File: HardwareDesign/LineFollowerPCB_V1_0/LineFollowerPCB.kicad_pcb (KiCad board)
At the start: 2 copper layers, 152 x 100 mm, 16 parts, among them J1 B2B-XH-A, J2 B4B-XH-A, J3 Conn_01x04, J4 Conn_01x02_Socket, M1 Motor_DC, M2 Motor_DC, U1 Black Pill v2, U2 DRV8833, U3 AMS1117-3.3, U4 SX1308

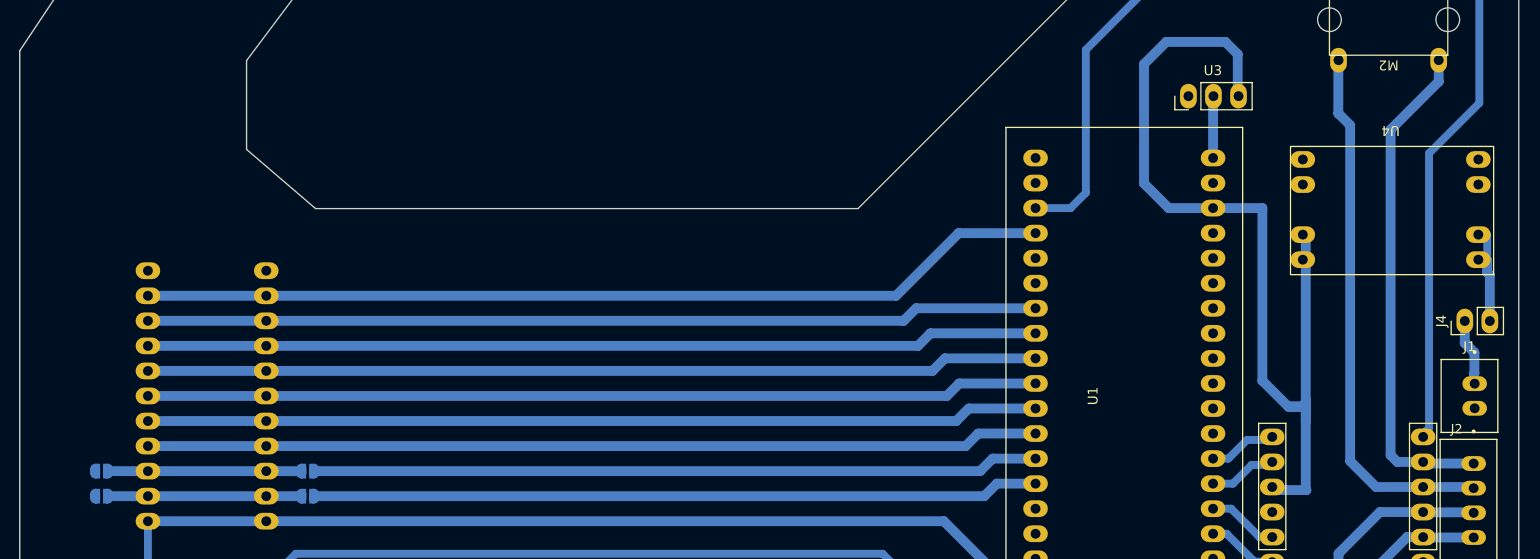
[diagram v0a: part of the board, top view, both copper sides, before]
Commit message: Add 1N4001 doide and connect the 5V power signal to the sensor
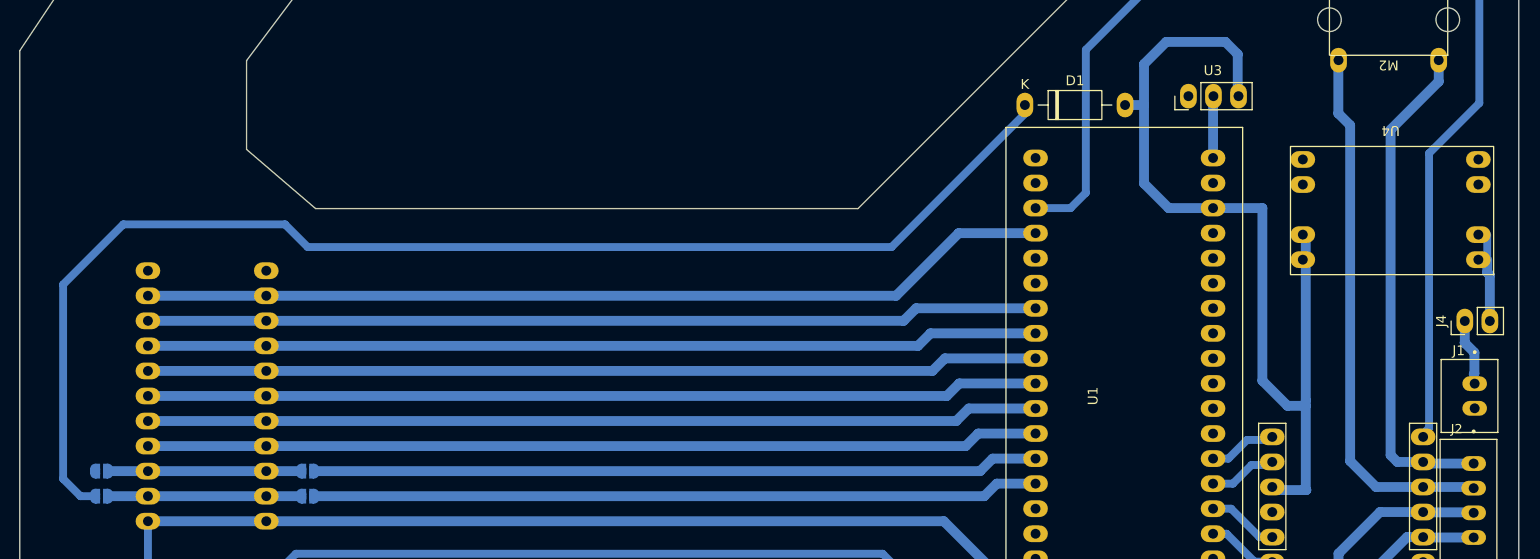
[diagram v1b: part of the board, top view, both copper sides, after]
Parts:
- added D1: 1N4001, Diode_THT:D_DO-41_SOD81_P10.16mm_Horizontal, F.Cu at (171.9, 59.5)
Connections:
- JP2 pad 1: 5.5V -> Net-(D1-K)
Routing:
- net Net-(D1-K): track 0.00 -> 131.2 mm
- net 5.5V: track 96.7 -> 94.9 mm

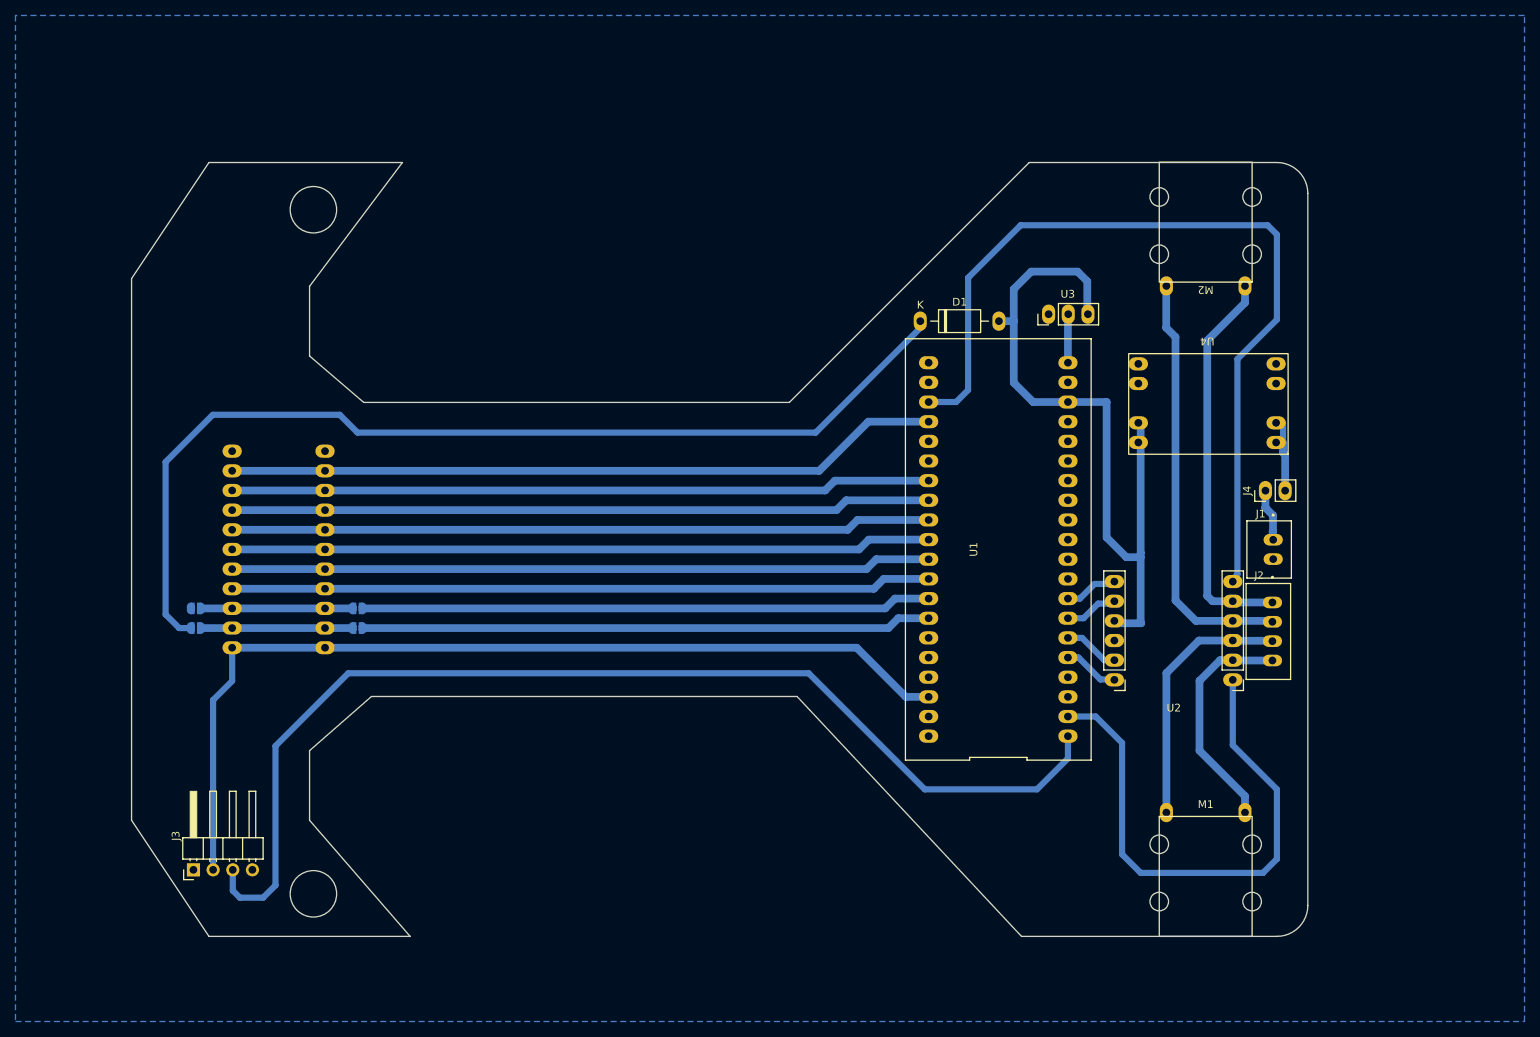
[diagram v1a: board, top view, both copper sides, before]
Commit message: Hardware changes: - Change the Neopixel pin to B15 instead of B12 - Add IR pinheader strip - Generate production files
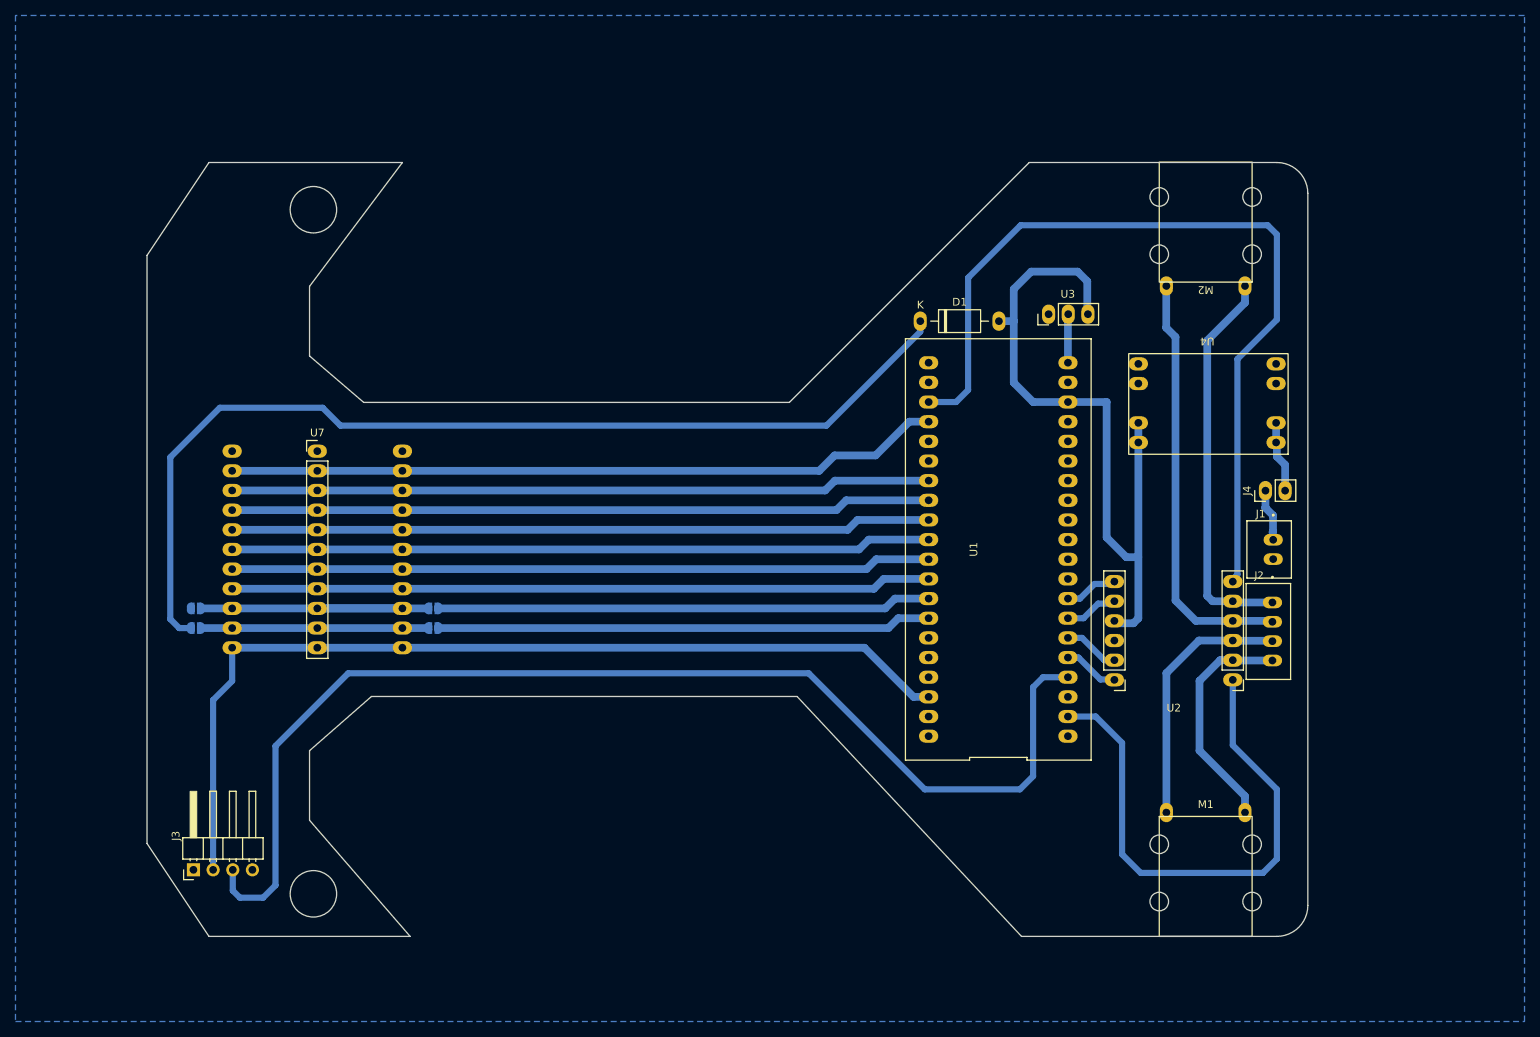
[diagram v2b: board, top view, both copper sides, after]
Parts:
- added U7: ~, Connector_PinHeader_2.54mm:PinHeader_1x11_P2.54mm_Vertical, F.Cu at (94.0, 76.3)
- moved U6 10.0 mm to (105.0, 76.3)
- moved JP1 9.80 mm to (109.0, 99.2)
- moved JP3 9.80 mm to (109.0, 96.6)
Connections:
- U1 pad 1: DI -> unconnected-(U1-PB12-Pad1)
- U1 pad 4: unconnected-(U1-PB15-Pad4) -> DI
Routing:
- net /SEL2: track 19.6 -> 39.4 mm
- net D8: track 73.7 -> 63.5 mm
- net D7: track 73.5 -> 63.5 mm
- net /SEL1: track 19.6 -> 29.4 mm
- net DI: track 144.3 -> 152.5 mm
- net 5.5V: track 94.9 -> 93.7 mm
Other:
- board size 152 x 100 mm -> 150 x 100 mm

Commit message: Hardware and software update: - Upuated STM32 and DC motors footprints - Updated the Gerber files - Implement P from the PID algorithm
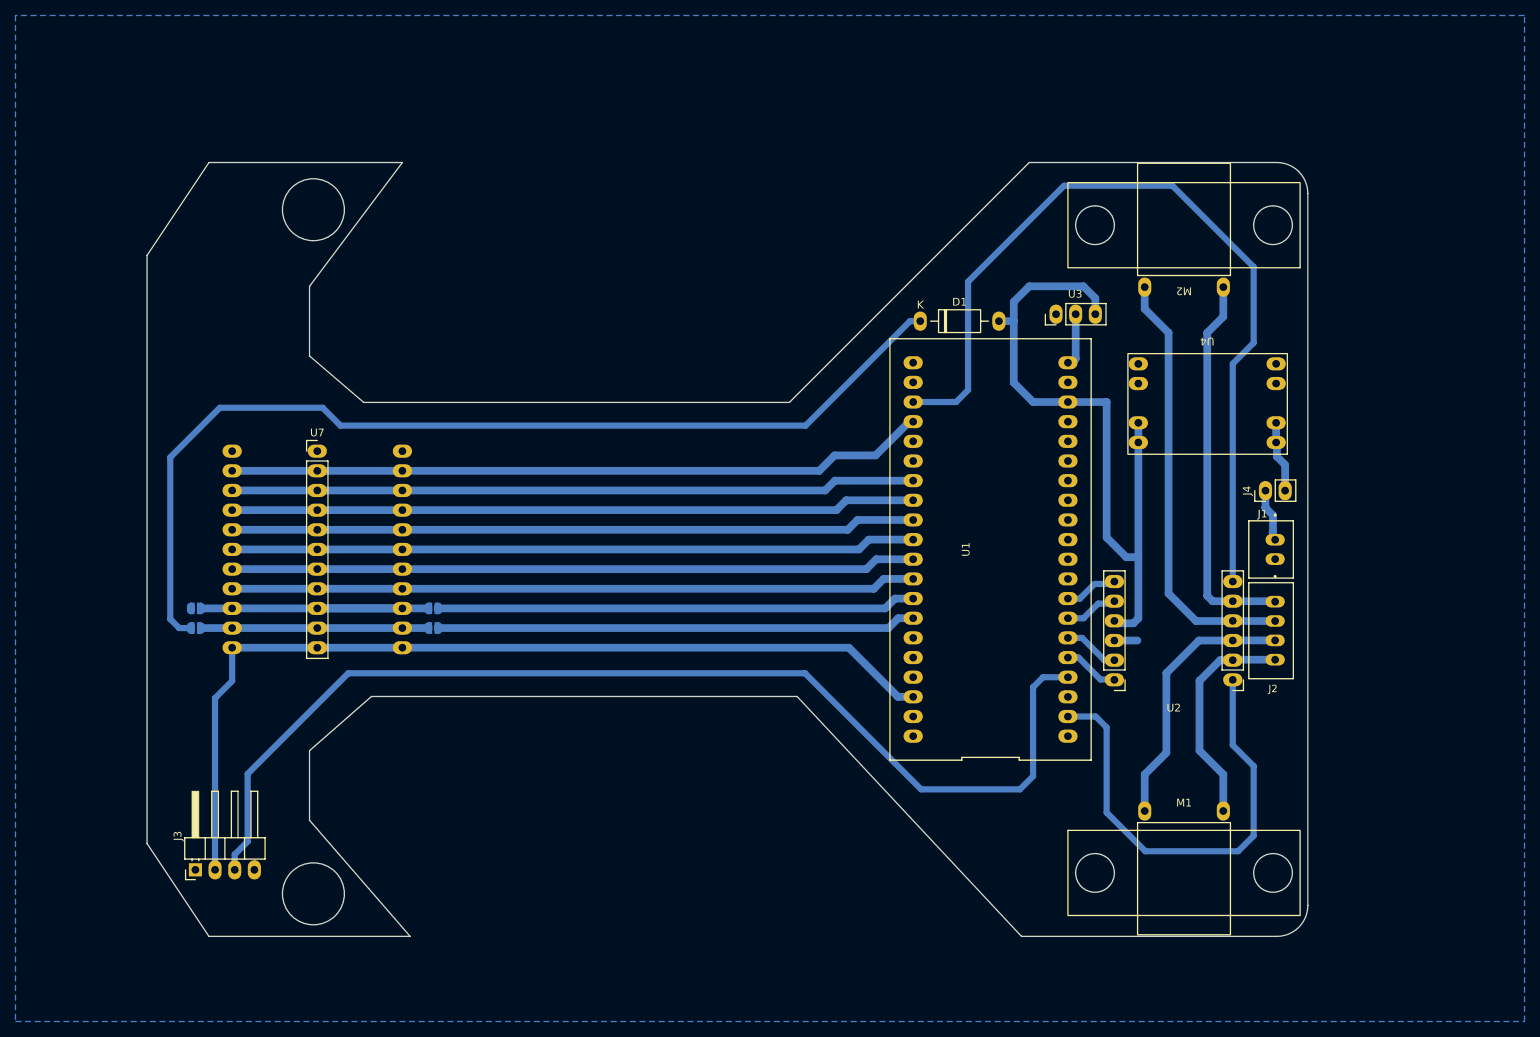
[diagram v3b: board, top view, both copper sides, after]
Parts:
- U4: value SX1308 -> Untitled
- moved M1 2.81 mm to (206.0, 130.8)
- moved M2 2.80 mm to (206.0, 47.1)
- moved U1 1.00 mm to (181.0, 89.0)
- moved U3 0.96 mm to (189.5, 58.6)
- moved J2 0.36 mm to (217.2, 99.5)
- moved J1 0.25 mm to (217.2, 89.0)
- moved J3 0.25 mm to (78.2, 130.4)
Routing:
- net SLEEP_SG: track 70.1 -> 59.8 mm
- net DI: track 152.5 -> 143.4 mm
- net GND: track 0.00 -> 2.98 mm
- net 5.5V: track 93.7 -> 90.9 mm
- net IR_3.3V: track 122.3 -> 120.2 mm
- net IR_SG: track 92.6 -> 90.6 mm
- net D8: track 63.5 -> 61.5 mm
- net D7: track 63.5 -> 61.5 mm
- net D6: track 90.5 -> 88.5 mm
- net D5: track 90.5 -> 88.5 mm
- net D4: track 90.5 -> 88.5 mm
- net D3: track 90.5 -> 88.5 mm
- net D2: track 90.5 -> 88.5 mm
- net D1: track 90.5 -> 88.5 mm
- net OUT3: track 55.3 -> 56.6 mm
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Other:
- outline, holes or cut-outs redrawn
